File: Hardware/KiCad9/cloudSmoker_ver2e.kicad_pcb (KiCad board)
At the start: 4 copper layers, 70 x 70 mm, 85 parts, among them J1 Conn_01x02_Pin, J11 Conn_01x04_Pin, J15 Conn_01x04_Pin, J3 Conn_01x04_Pin, J6 Conn_01x04_Pin, J7 Conn_01x05, Q1 BSS138, Q2 BSS138, SW2 SW_Push_Dual, SW3 SW_Push_Dual, U1 TLV76733DGNR, U2 GT-USB-7010ASV, U3 INA226AIDGSR, U4 ESP32-C3-WROOM-02U-N4, U5 SRV05-4-P-T7, U6 ADS1115IRUGR, U7 SRV05-4-P-T7

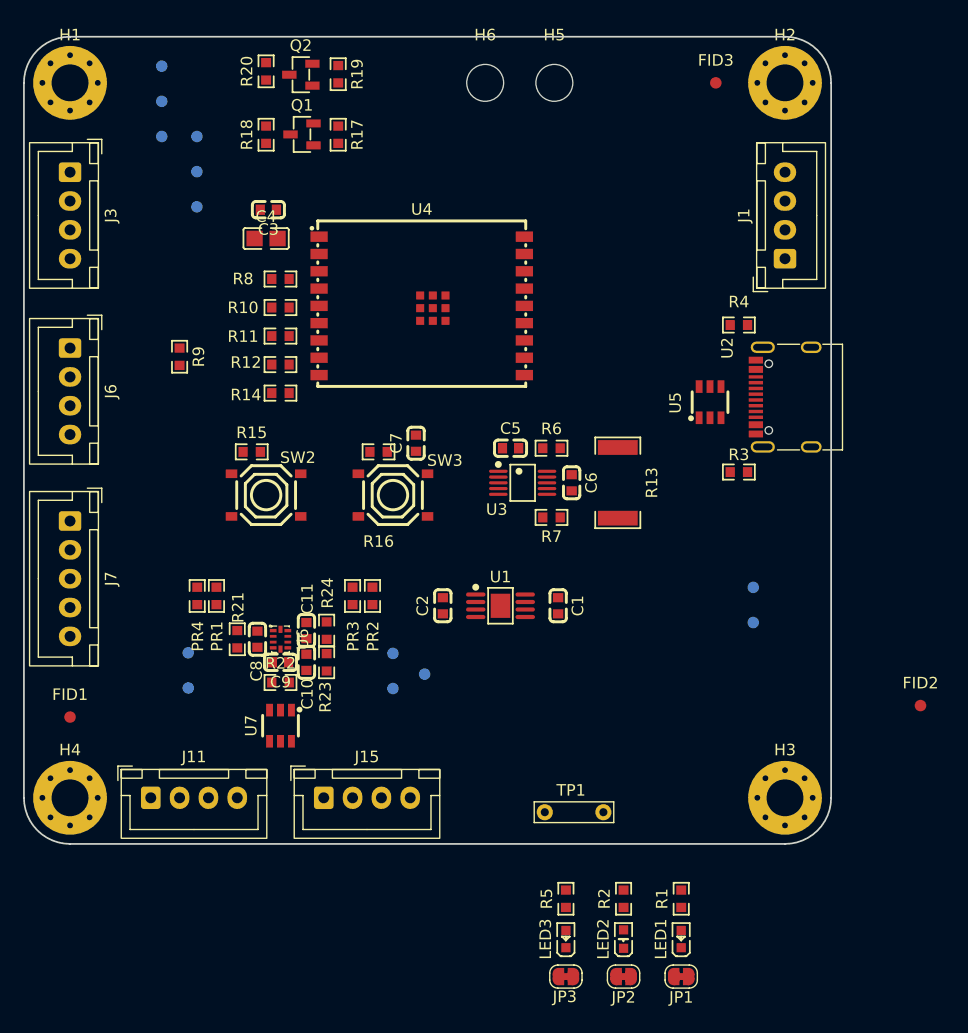
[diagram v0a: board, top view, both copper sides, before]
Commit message: update hardware files for version 2e
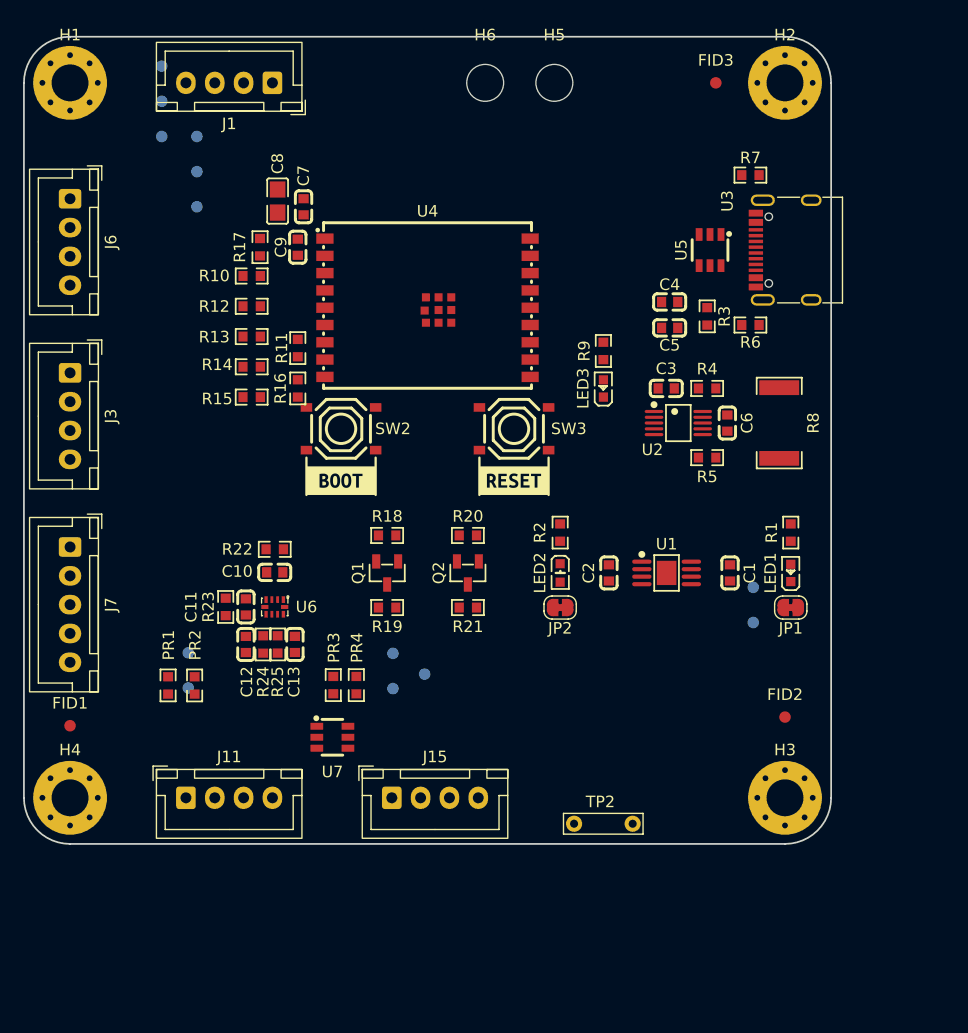
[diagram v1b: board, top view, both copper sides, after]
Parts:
- removed JP3: SolderJumper_2_Bridged, Jumper:SolderJumper-2_P1.3mm_Bridged_RoundedPad1.0x1.5mm
- added C4: 470nF, JLCImport:CC0603KRX7R9BB104, F.Cu at (150.0, 83.0)
- added C5: 470nF, JLCImport:CC0603KRX7R9BB104, F.Cu at (150.0, 85.2)
- added R3: 0 ohm, JLCImport:PTFR0603B120KP9, F.Cu at (153.2, 84.2)
- added kibuzzard-6A0E9251: G***, kibuzzard-6A0E9251, F.Cu at (136.5, 98.5)
- added kibuzzard-6A0E9267: G***, kibuzzard-6A0E9267, F.Cu at (121.5, 98.5)
- moved R21 49.7 mm to (132.5, 109.5), turned to 180 degrees
- moved LED3 47.9 mm to (144.2, 90.5)
- moved R9 47.6 mm to (144.2, 87.2)
- moved J1 47.0 mm to (115.5, 64.0), turned to 180 degrees
- moved Q2 45.6 mm to (132.5, 106.5), turned to 90 degrees
- moved R19 42.3 mm to (125.5, 109.5), turned to 180 degrees
- moved R20 41.6 mm to (132.5, 103.2), turned to 0 degrees
- moved Q1 38.7 mm to (125.5, 106.5), turned to 90 degrees
- moved R18 35.0 mm to (125.5, 103.2), turned to 0 degrees
- moved JP1 33.4 mm to (160.5, 109.5)
- moved LED1 33.1 mm to (160.5, 106.5)
- moved R1 33.1 mm to (160.5, 103.0)
- moved JP2 32.5 mm to (140.5, 109.5)
- moved LED2 32.2 mm to (140.5, 106.5), turned to -90 degrees
- moved R2 32.2 mm to (140.5, 103.0), turned to -90 degrees
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- renumbered C8 to C10, C9 to C11, C10 to C12, C11 to C13, C5 to C3, C3 to C7, C4 to C8, C7 to C9, R8 to R10, R9 to R11, R10 to R12, R11 to R13, R12 to R14, R14 to R15, R15 to R16, R16 to R17, R17 to R18, R18 to R19, R19 to R20, R20 to R21, R21 to R22, R22 to R23, R23 to R24, R24 to R25, R6 to R4, R7 to R5, R3 to R6, R4 to R7, R13 to R8, R5 to R9, TP5 to TP1, TP1 to TP2, TP6 to TP3, TP2 to TP4, TP3 to TP5, TP4 to TP6, U3 to U2, U2 to U3
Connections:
- LED3 pad 1: Net-(JP3-A) -> GND
- R14 pad 2: Net-(U4-IO8) -> DISP_CS
- R6 pad 1: Net-(U2-CC1) -> Net-(U3-CC1)
- R7 pad 1: Net-(U2-CC2) -> Net-(U3-CC2)
- U3 pad A5: Net-(U2-CC1) -> Net-(U3-CC1)
- U3 pad B5: Net-(U2-CC2) -> Net-(U3-CC2)
- U4 pad 7: Net-(U4-IO8) -> DISP_CS
- U5 pad 3: Net-(U2-CC1) -> unconnected-(U5-IO2-Pad3)
- U5 pad 4: Net-(U2-CC2) -> unconnected-(U5-IO3-Pad4)
- U5 pad 5: +5V -> VBUS
